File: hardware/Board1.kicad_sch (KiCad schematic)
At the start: 20 parts, among them IC1 AH1912-W-7, J1 DX07S016JA3R1500, J2 Conn_01x04_Pin, J3 Conn_ST_STDC14, J4 Conn_01x02_Pin, SW1 SW_Push, U1 STM32F042G6U6TR, U2 TS2940CW33_RPG, U4 TJA1051T-3

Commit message: Comments Added
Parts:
- added BT1: XT30, Connector_AMASS:AMASS_XT30PW-M_1x02_P2.50mm_Horizontal, symbol Device:Battery_Cell
- J2: footprint Connector_PinHeader_2.00mm:PinHeader_1x04_P2.00mm_Vertical -> Connector_JST:JST_EH_S4B-EH_1x04_P2.50mm_Horizontal
- J4: footprint Connector_PinHeader_2.00mm:PinHeader_1x02_P2.00mm_Vertical_SMD_Pin1Right -> (none)
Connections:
- net +3.3V: no longer D1.1 (K), D2.1 (K)
- net +3V3: no longer D2.2 (A)
- net GND: now also BT1.2 (-); no longer J4.2 (Pin_2)
- net at J1.5 (D-): now also J1.8 (D-)
- net at J1.6 (D+): now also J1.7 (D+)
- net +3.3VA: no longer names the net of J4.1 (Pin_1)
- net +3.3VA: no longer D1.2 (A)
- new net: D1.1 (K), D2.1 (K)
- new net +BATT: BT1.1 (+), D2.2 (A)
- no-connect marks 27 -> 23
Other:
- note added: "5V A"
- note added: "5VA"
- note added: "NEED ANOTHER PROB 2X01 JST HEADER FOR CANH AND CANL IN (DAISY CHAIN CONFIGURATION BETWEEN BOARDS)"
- note added: "battery 5V"
- note added: "changed footprint to JST EH 2.50mm"
- note added: "the motherboard will deliver **5V** of voltage into each board and then each board is required to regulated the voltage locally according to you own circuit"

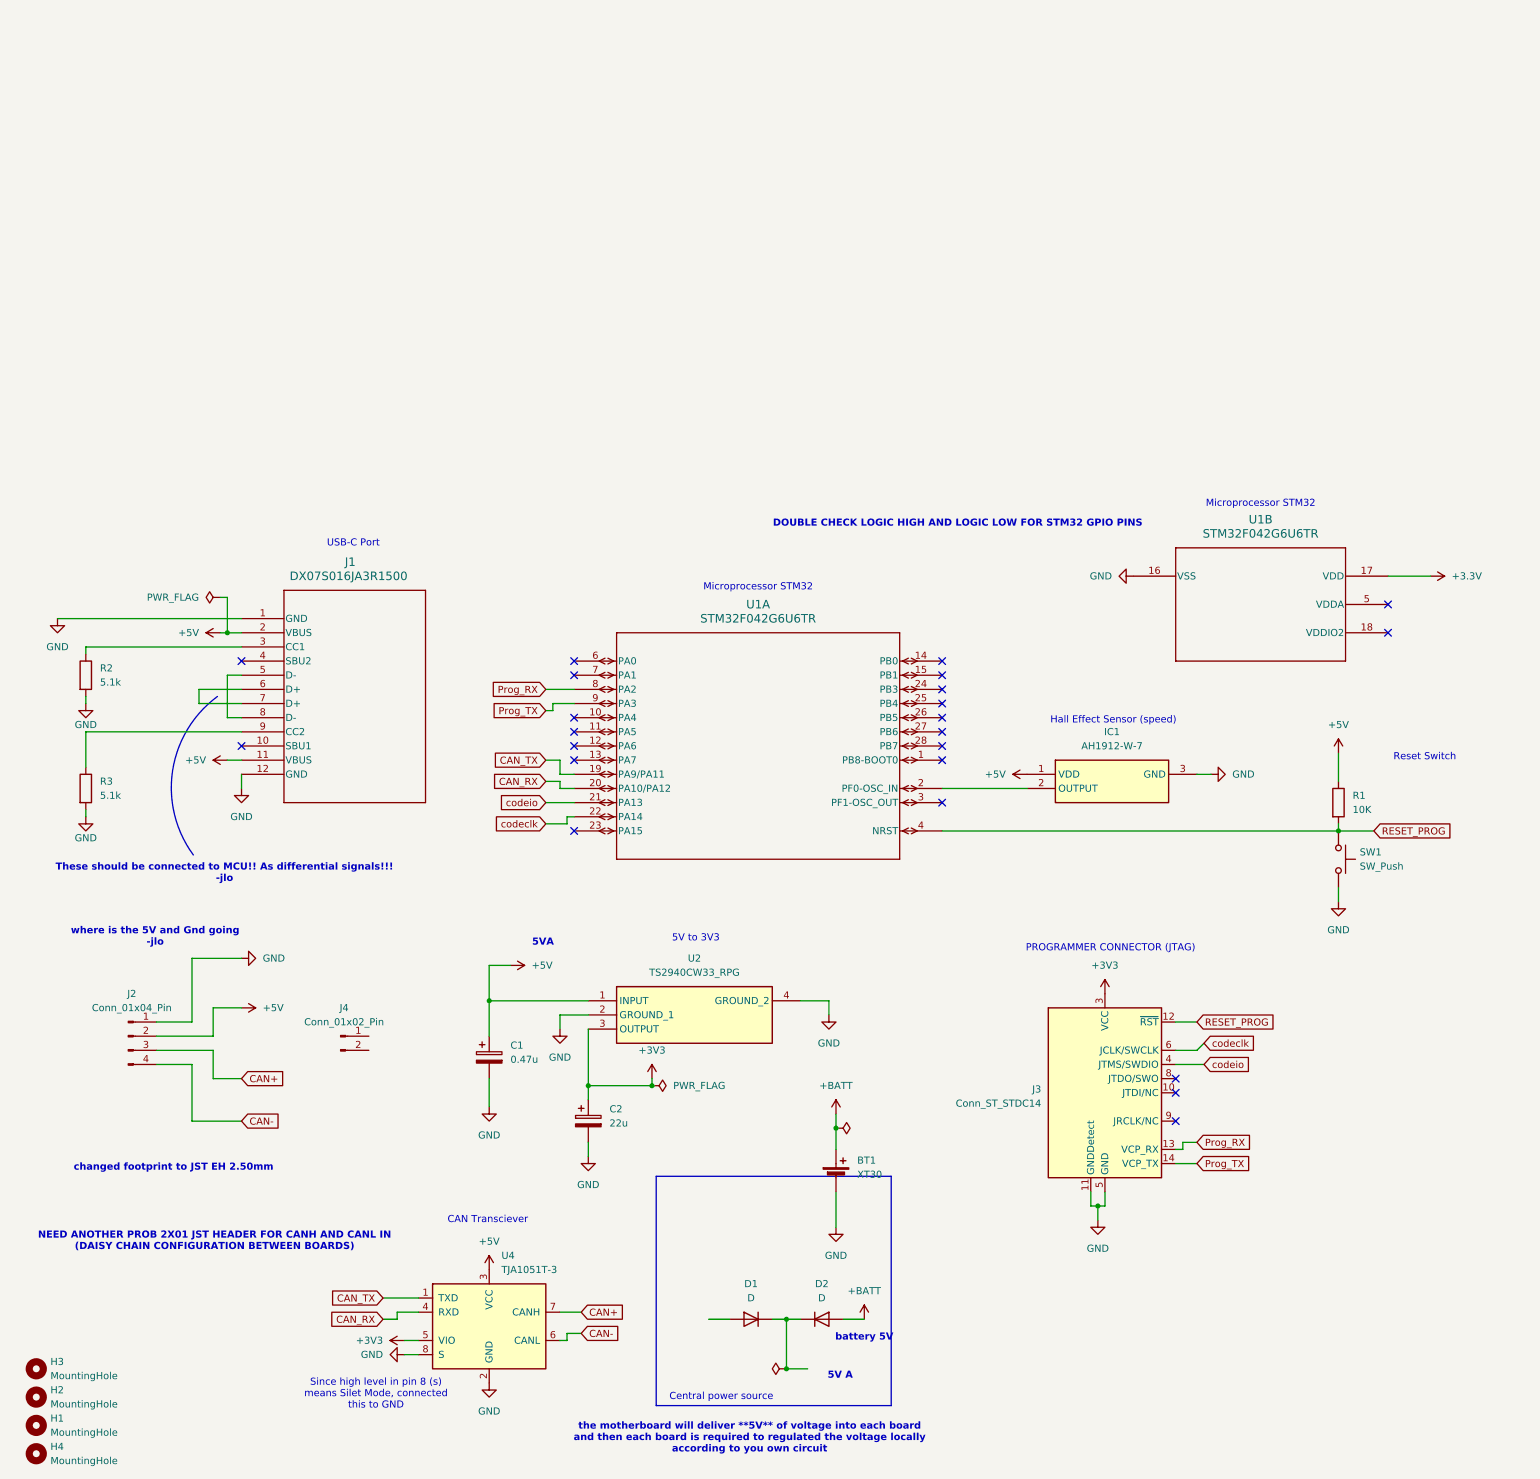
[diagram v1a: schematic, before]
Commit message: Modified Schematic according to comments/meeting
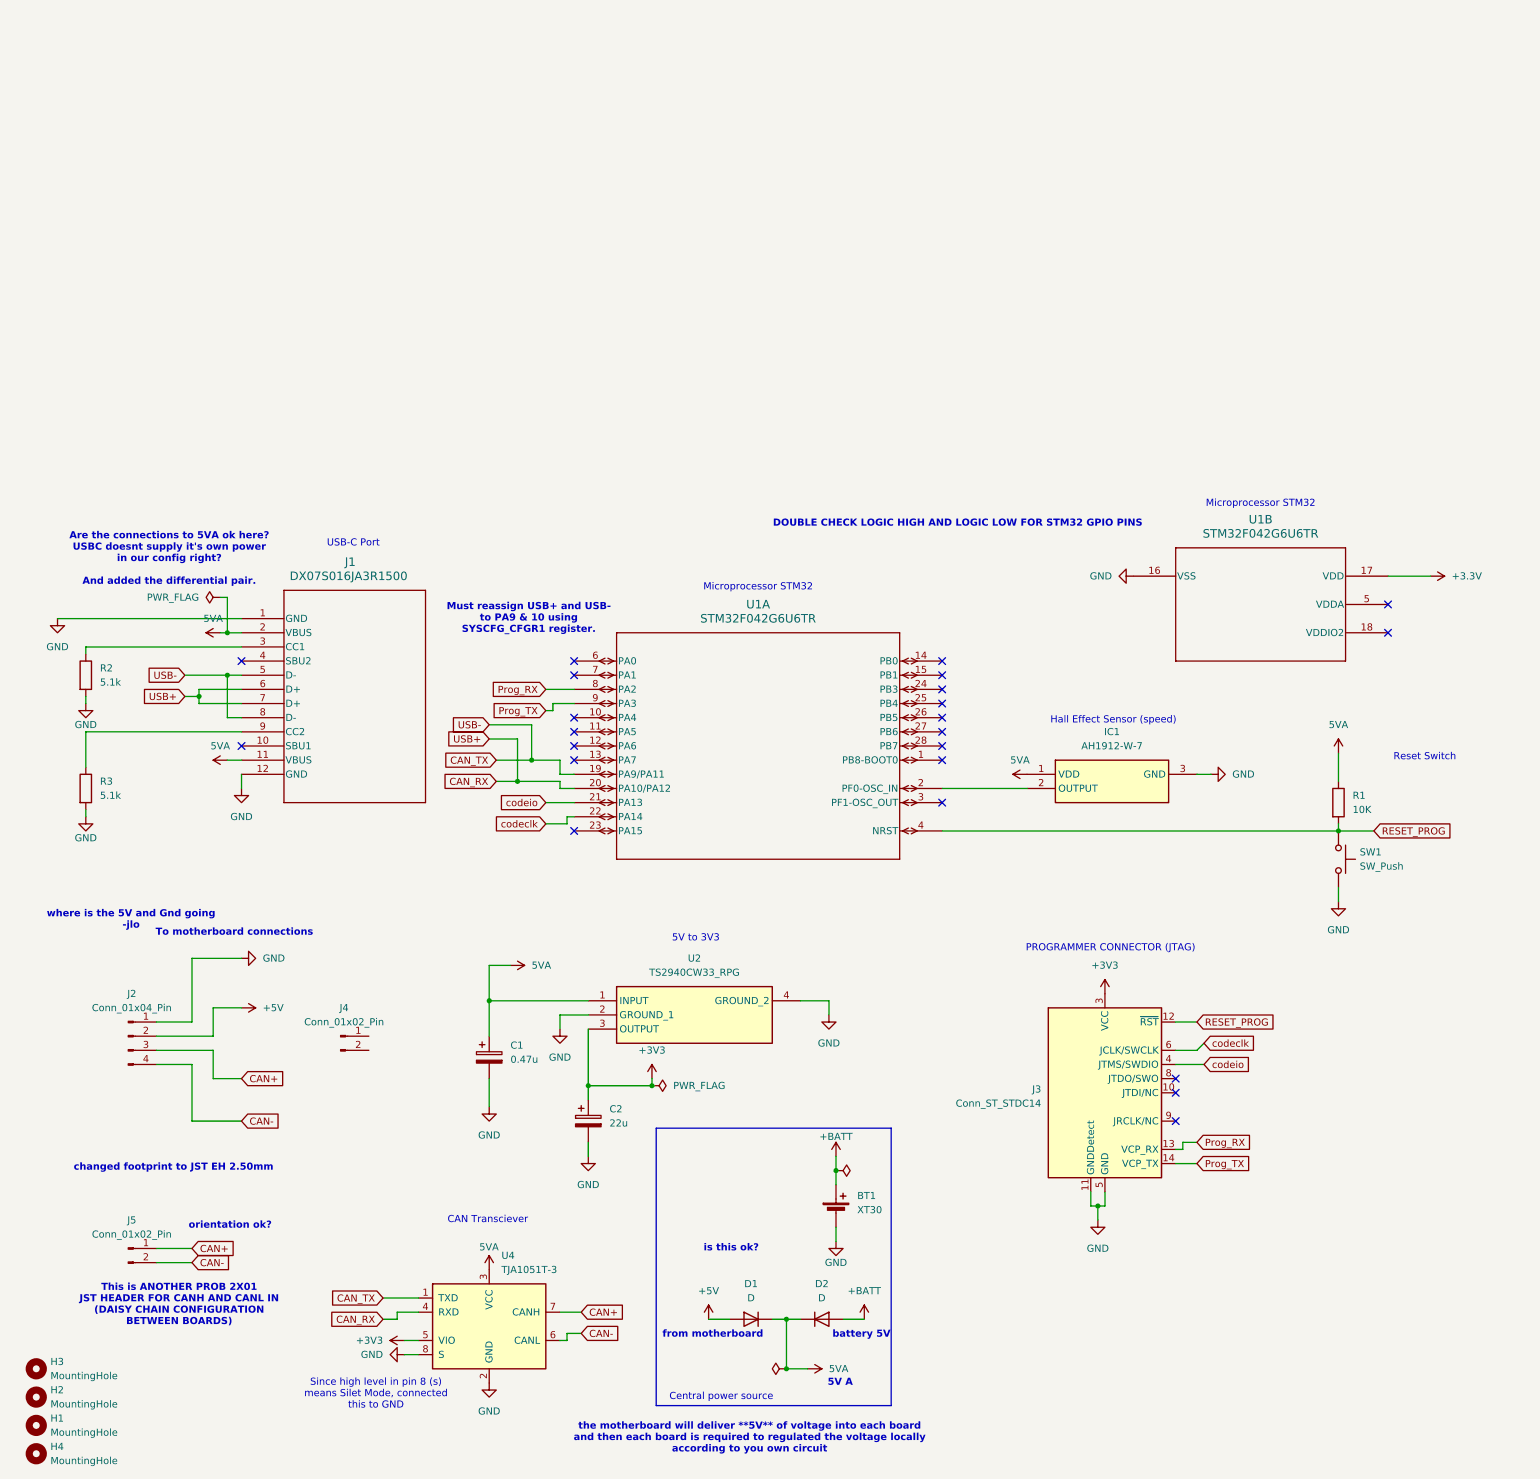
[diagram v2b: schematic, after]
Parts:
- added J5: Conn_01x02_Pin, Connector_JST:JST_EH_S2B-EH_1x02_P2.50mm_Horizontal, symbol Connector:Conn_01x02_Pin
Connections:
- net +5V: now also D1.2 (A); no longer C1.1, IC1.1 (VDD), J1.11 (VBUS), J1.2 (VBUS), R1.1, U2.1 (INPUT), U4.3 (VCC)
- net CAN+: now also J5.1 (Pin_1)
- net CAN-: now also J5.2 (Pin_2)
- net CAN_RX: now also J1.6 (D+), J1.7 (D+)
- net CAN_TX: now also J1.5 (D-), J1.8 (D-)
- net 5VA: now reaches D1.1 (K), D2.1 (K)
- net 5VA: now also C1.1, IC1.1 (VDD), J1.11 (VBUS), J1.2 (VBUS), R1.1, U2.1 (INPUT), U4.3 (VCC)
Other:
- note added: "Are the connections to 5VA ok here? USBC doesnt supply it's own power in our config right? And added the differential pair."
- note added: "Must reassign USB+ and USB- to PA9 & 10 using SYSCFG_CFGR1 register."
- note added: "This is ANOTHER PROB 2X01 JST HEADER FOR CANH AND CANL IN (DAISY CHAIN CONFIGURATION BETWEEN BOARDS)"
- note added: "To motherboard connections"
- note added: "from motherboard"
- note added: "is this ok?"
- note added: "orientation ok?"
- note removed: "5VA"
- note removed: "NEED ANOTHER PROB 2X01 JST HEADER FOR CANH AND CANL IN (DAISY CHAIN CONFIGURATION BETWEEN BOARDS)"
- note removed: "These should be connected to MCU!! As differential signals!!! -jlo"
- company: By Evelyn Koszta and Eun Gu Kang -> By Evelyn Koszta 
- moved on the sheet: BT1

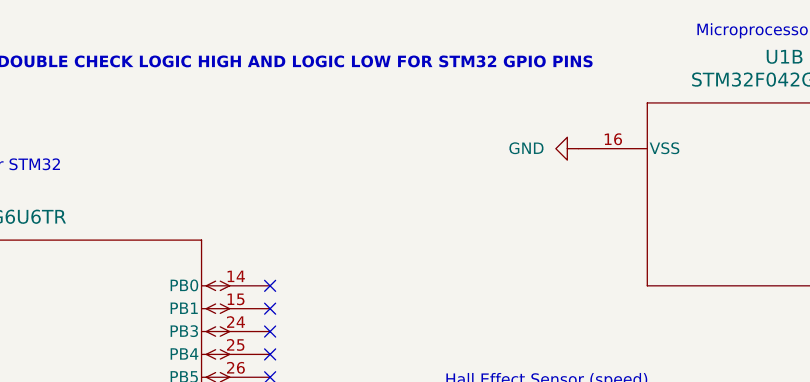
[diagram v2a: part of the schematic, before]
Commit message: Updated board schematic with comments
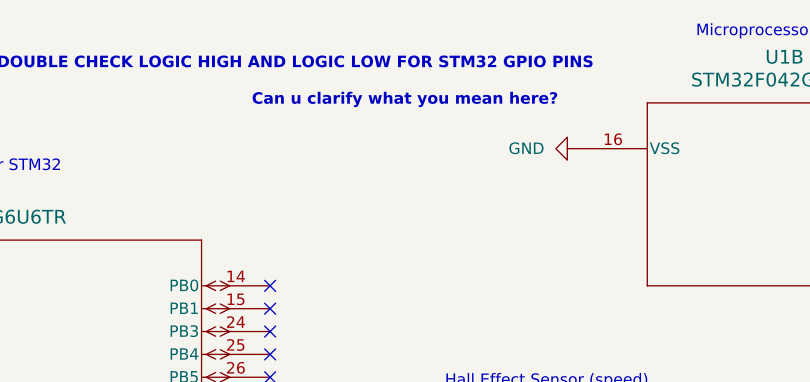
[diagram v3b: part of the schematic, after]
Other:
- note added: "Can u clarify what you mean here?"
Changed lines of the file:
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@@
+		)
+	)
+	(text "Can u clarify what you mean here?"
+		(exclude_from_sim no)
+		(at 192.786 31.496 0)
+		(effects
+			(font
+				(size 1.27 1.27)
+				(bold yes)
+				(color 255 153 60 1)
+			)
 		)
 	)

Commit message: Made a few changes regarding STM32
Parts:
- removed D1, D2: D, Diode_SMD:D_SOD-123, symbol Device:D
- removed J1: DX07S016JA3R1500, CONN12_DX07S_JAE, symbol DX07S016JA3R1500_USBC:DX07S016JA3R1500
- removed J2: Conn_01x04_Pin, Connector_JST:JST_EH_S4B-EH_1x04_P2.50mm_Horizontal, symbol Connector:Conn_01x04_Pin
- removed R3: 5.1k, Resistor_SMD:R_0603_1608Metric, symbol Device:R
- added C10, C11, C4, C5, C6, C7: 100n, Capacitor_SMD:C_0603_1608Metric, symbol Device:C
- added C3: 4.7n, Capacitor_SMD:C_0603_1608Metric, symbol Device:C
- added C8: 10n, Capacitor_SMD:C_0603_1608Metric, symbol Device:C
- added C9: 1u, Capacitor_SMD:C_0603_1608Metric, symbol Device:C
- added D1, D2, D3: D_Schottky, Diode_SMD:D_SOD-123, symbol Device:D_Schottky
- added IC2: AH1912-W-7, Package_TO_SOT_SMD:SC-59, symbol AH1912-W-7:AH1912-W-7
- added J2: USB_C_Receptacle_USB2.0, Connector_USB:USB_C_Receptacle_HRO_TYPE-C-31-M-12, symbol Connector:USB_C_Receptacle_USB2.0_16P
- added R4, R5: 60, Resistor_SMD:R_0603_1608Metric, symbol Device:R
- added R6, R7: 22, Resistor_SMD:R_0603_1608Metric, symbol Device:R
- added R8, R9: 5.1K, Resistor_SMD:R_0603_1608Metric, symbol Device:R
- added SW2: SW_Push, Button_Switch_SMD:SW_SPST_SKQG_WithStem, symbol Switch:SW_Push
- added U3: STM32F072RBTx, Package_QFP:LQFP-64_10x10mm_P0.5mm, symbol MCU_ST_STM32F0:STM32F072RBTx
- added Y1: 8M, Crystal:Resonator_SMD_Murata_CSTxExxV-3Pin_3.0x1.1mm, symbol Device:Resonator
- J4: footprint (none) -> Connector_JST:JST_EH_S2B-EH_1x02_P2.50mm_Horizontal
- R2: value 5.1k -> 10K
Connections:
- net +3.3V: now also R2.1, C10.2, C11.2, C4.2, C5.2, C6.2, C7.2, C8.2, C9.2, U3.1 (VBAT), U3.13 (VDDA), U3.19 (VDD), U3.32 (VDD), U3.48 (VDDIO2), U3.64 (VDD)
- net +5V: now also J4.2 (Pin_2), D2.2 (A)
- net +BATT: now also D1.2 (A)
- net 5VA: now also D1.1 (K), D2.1 (K), D3.1 (K), IC2.1 (VDD)
- net CAN+: now also R4.1
- net CAN-: now also R5.2
- net CAN_RX: now also R7.1, U3.45 (PA12), U3.50 (PA15)
- net CAN_TX: now also R6.1, U3.44 (PA11), U3.49 (PA14)
- net GND: now also J4.1 (Pin_1), C10.1, C11.1, C3.2, C4.1, C5.1, C6.1, C7.1, C8.1, C9.1, IC2.3 (GND), J2.A1 (GND), J2.A12 (GND), J2.B1 (GND), J2.B12 (GND), R8.1, R9.1, SW2.2, U3.12 (VSSA), U3.18 (VSS), U3.31 (VSS), U3.47 (VSS), U3.60 (BOOT0), U3.63 (VSS), Y1.2; no longer R2.2
- net Prog_RX: now also U3.17 (PA3)
- net Prog_TX: now also U3.16 (PA2)
- net RESET_PROG: now also R2.2, SW2.1, U3.7 (NRST)
- new net: C3.1, R4.2, R5.1
- new net: U3.5 (PF0), Y1.1
- new net: U3.6 (PF1), Y1.3
- new net: J2.B5 (CC2), R9.2
- new net: IC2.2 (OUTPUT), U3.27 (PB1)
- new net: J2.A5 (CC1), R8.2
- new net +5VD: D3.2 (A), J2.A4 (VBUS), J2.A9 (VBUS), J2.B4 (VBUS), J2.B9 (VBUS)
- new net D+: J2.A6 (D+), J2.B6 (D+), R7.2
- new net D-: J2.A7 (D-), J2.B7 (D-), R6.2
- no-connect marks 23 -> 24
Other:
- note added: "5V - 3.3V Regulator"
- note added: "To Motherboard"
- note added: "To env sensor board"
- note added: "USB Type-C"
- note removed: "5V A"
- note removed: "Are the connections to 5VA ok here? USBC doesnt supply it's own power in our config right? And added the differential pair."
- note removed: "Can u clarify what you mean here?"
- note removed: "DOUBLE CHECK LOGIC HIGH AND LOGIC LOW FOR STM32 GPIO PINS"
- note removed: "This is ANOTHER PROB 2X01 JST HEADER FOR CANH AND CANL IN (DAISY CHAIN CONFIGURATION BETWEEN BOARDS)"
- note removed: "To motherboard connections"
- note removed: "USB-C Port"
- note removed: "changed footprint to JST EH 2.50mm"
- note removed: "is this ok?"
- note removed: "orientation ok?"
- note removed: "where is the 5V and Gnd going -jlo"
- moved on the sheet: BT1, C1, C2, J5, U2, U4
